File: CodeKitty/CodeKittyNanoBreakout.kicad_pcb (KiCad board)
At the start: 2 copper layers, 17.8 x 43.2 mm, 18 parts, among them P1 CONN_01X02, P2 CONN_01X02, P3 CONN_01X03, P4 CONN_01X03, P5 CONN_01X03, Q1 MMBT3904, SW1 SW_PUSH_SMALL_H, SW2 Switch_SPDT_x2, U1 ArduinoNano

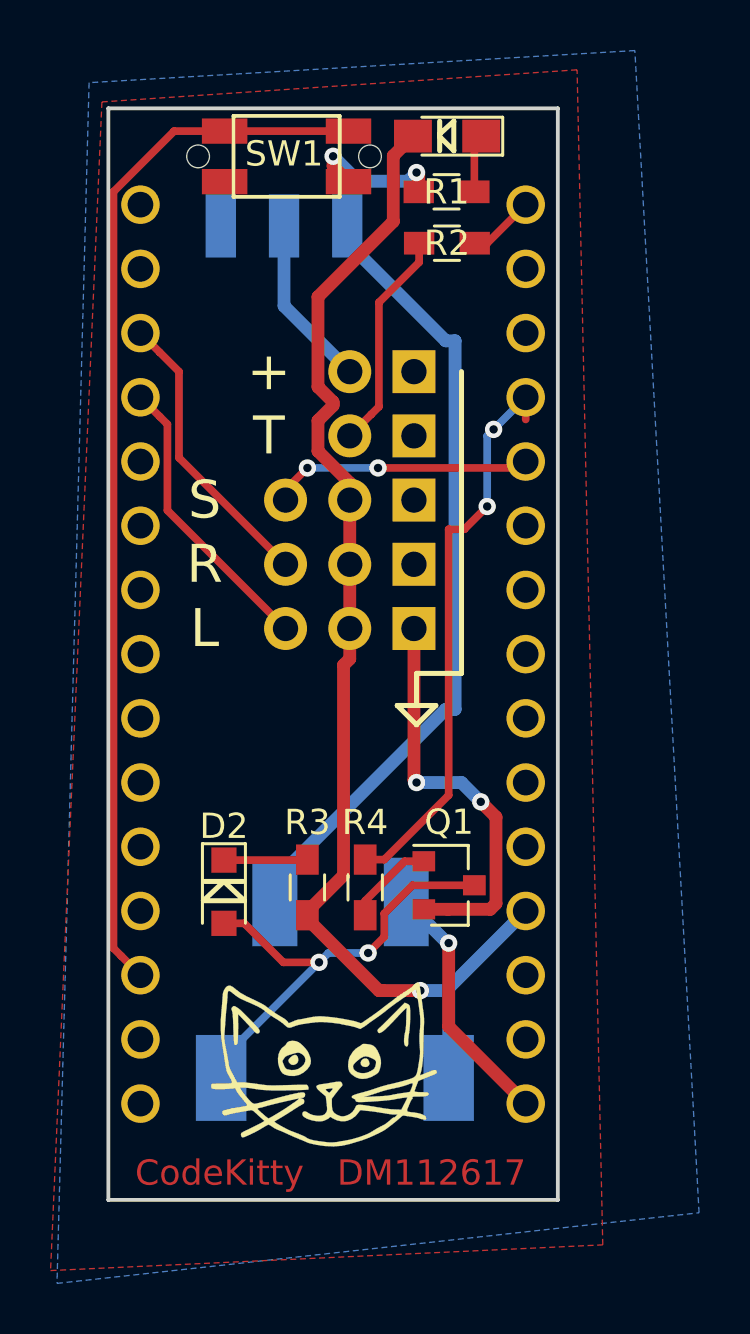
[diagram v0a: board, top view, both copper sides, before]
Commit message: fixed CKN
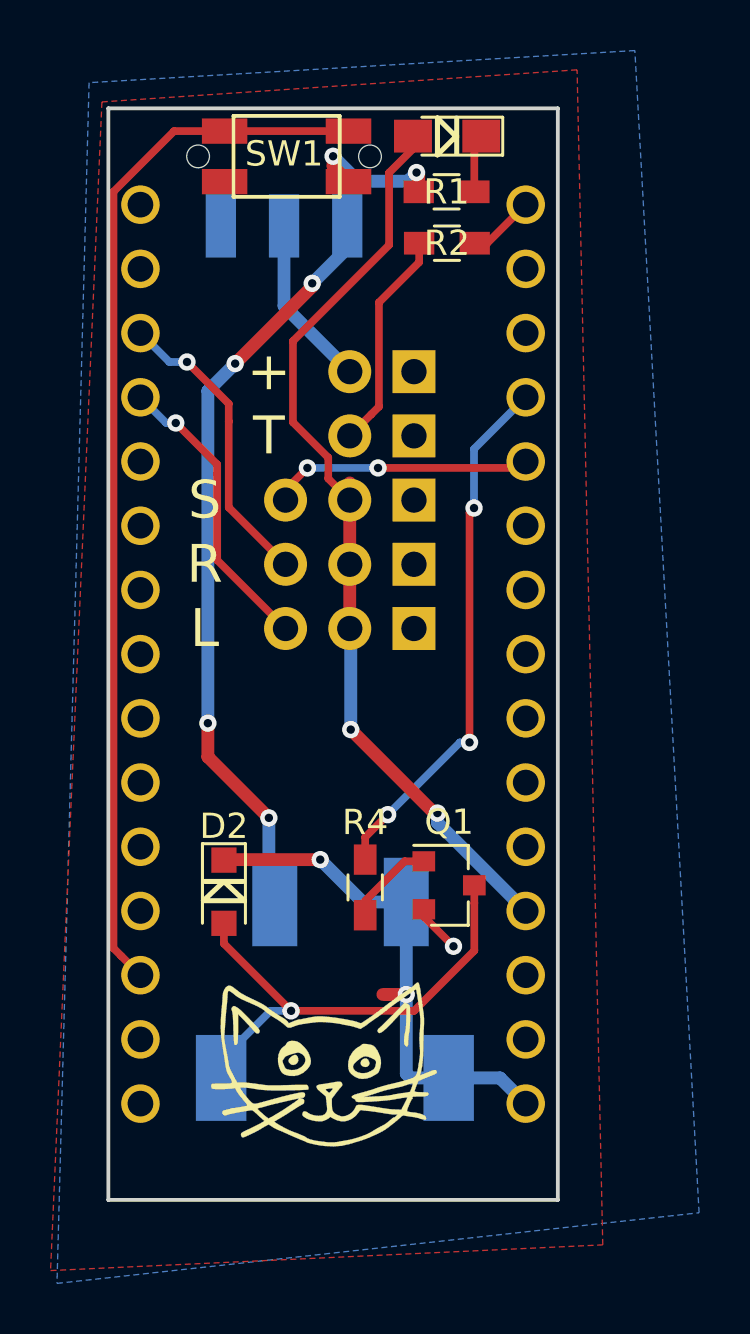
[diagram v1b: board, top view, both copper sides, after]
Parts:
- removed R3: R, Resistors_SMD:R_0603_HandSoldering
- R4: value R -> 1K
- SP1: value SPEAKER -> PIEZO
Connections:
- D2 pad 1: Net-(D2-Pad1) -> VCC
- SP1 pad 1: 5V -> VCC
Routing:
- net GND: track 22.1 -> 7.86 mm, vias 4 -> 3
- net 5V: track 48.9 -> 37.2 mm, vias 1 -> 2
- net VCC: track 9.96 -> 20.9 mm, vias 1 -> 2
- net Net-(D2-Pad1): track 3.31 -> 0.00 mm
- net BUZZ: track 22.6 -> 21.1 mm, vias 2 -> 3
- net Net-(D2-Pad2): track 18.5 -> 19.7 mm, vias 2 -> 1
- net RSERVO: track 11.5 -> 11.9 mm, vias 0 -> 1
- net Net-(F1-Pad1): track 31.9 -> 31.6 mm, vias 0 -> 4
- net LSERVO: track 11.5 -> 11.7 mm, vias 0 -> 1
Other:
- board text added: "CodeKitty v1.0 DM120317"
- board text removed: "CodeKitty DM112617"
